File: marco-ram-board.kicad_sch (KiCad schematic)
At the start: 0 parts

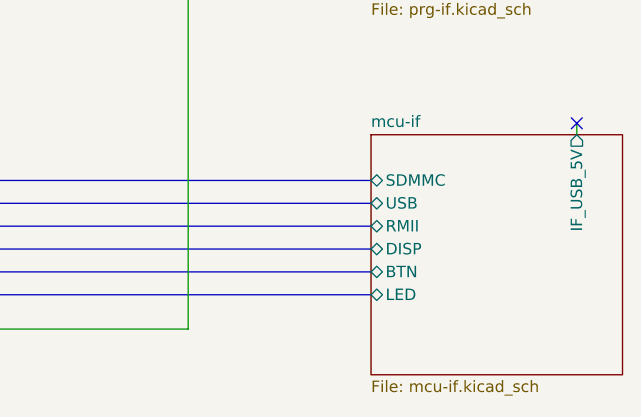
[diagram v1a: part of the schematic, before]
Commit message: Fix led current limiting resistor values.
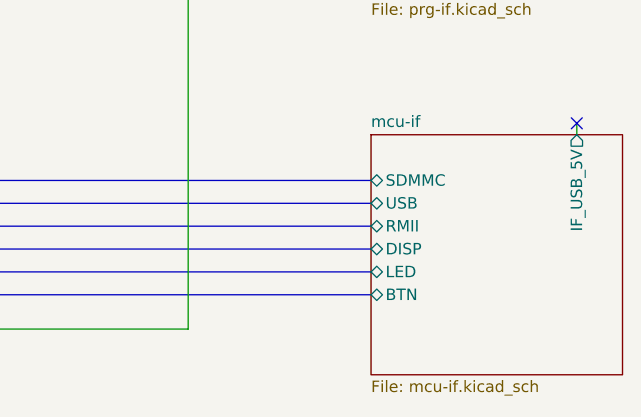
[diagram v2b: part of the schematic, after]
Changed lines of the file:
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@@
+    (stroke (width 0) (type default) (color 0 0 0 0))
+  )
+  (bus (pts (xy 163.83 82.55) (xy 208.28 82.55))
+    (stroke (width 0) (type default) (color 0 0 0 0))
+  )
+  (wire (pts (xy 231.14 118.11) (xy 231.14 119.38))
+    (stroke (width 0) (type default) (color 0 0 0 0))
+  )
+  (wire (pts (xy 187.96 140.97) (xy 163.83 140.97))
+    (stroke (width 0) (type default) (color 0 0 0 0))
+  )
+  (wire (pts (xy 187.96 99.06) (xy 208.28 99.06))
+    (stroke (width 0) (type default) (color 0 0 0 0))
+  )
+  (wire (pts (xy 163.83 87.63) (xy 208.28 87.63))
+    (stroke (width 0) (type default) (color 0 0 0 0))
+  )
+  (bus (pts (xy 105.41 82.55) (xy 125.73 82.55))
+    (stroke (width 0) (type default) (color 0 0 0 0))
+  )
+  (bus (pts (xy 163.83 134.62) (xy 208.28 134.62))
+    (stroke (width 0) (type default) (color 0 0 0 0))
+  )
+  (bus (pts (xy 163.83 132.08) (xy 208.28 132.08))
+    (stroke (width 0) (type default) (color 0 0 0 0))
+  )
+  (bus (pts (xy 163.83 127) (xy 208.28 127))
+    (stroke (width 0) (type default) (color 0 0 0 0))
+  )
+  (bus (pts (xy 163.83 129.54) (xy 208.28 129.54))
+    (stroke (width 0) (type default) (color 0 0 0 0))
+  )
+  (wire (pts (xy 163.83 90.17) (xy 208.28 90.17))
+    (stroke (width 0) (type default) (color 0 0 0 0))
+  )
+  (wire (pts (xy 231.14 76.2) (xy 231.14 77.47))
     (stroke (width 0) (type default) (color 0 0 0 0))
   )
   (bus (pts (xy 163.83 137.16) (xy 208.28 137.16))
-    (stroke (width 0) (type default) (color 0 0 0 0))
-  )
-  (bus (pts (xy 163.83 82.55) (xy 208.28 82.55))
-    (stroke (width 0) (type default) (color 0 0 0 0))
-  )
-  (wire (pts (xy 231.14 118.11) (xy 231.14 119.38))
-    (stroke (width 0) (type default) (color 0 0 0 0))
-  )
-  (wire (pts (xy 187.96 140.97) (xy 163.83 140.97))
-    (stroke (width 0) (type default) (color 0 0 0 0))
-  )
-  (wire (pts (xy 187.96 99.06) (xy 208.28 99.06))
-    (stroke (width 0) (type default) (color 0 0 0 0))
-  )
-  (wire (pts (xy 163.83 87.63) (xy 208.28 87.63))
-    (stroke (width 0) (type default) (color 0 0 0 0))
-  )
-  (bus (pts (xy 105.41 82.55) (xy 125.73 82.55))
-    (stroke (width 0) (type default) (color 0 0 0 0))
-  )
-  (bus (pts (xy 163.83 134.62) (xy 208.28 134.62))
-    (stroke (width 0) (type default) (color 0 0 0 0))
-  )
-  (bus (pts (xy 163.83 132.08) (xy 208.28 132.08))
-    (stroke (width 0) (type default) (color 0 0 0 0))
-  )
-  (bus (pts (xy 163.83 127) (xy 208.28 127))
-    (stroke (width 0) (type default) (color 0 0 0 0))
-  )
-  (bus (pts (xy 163.83 129.54) (xy 208.28 129.54))
-    (stroke (width 0) (type default) (color 0 0 0 0))
-  )
-  (wire (pts (xy 163.83 90.17) (xy 208.28 90.17))
-    (stroke (width 0) (type default) (color 0 0 0 0))
-  )
-  (wire (pts (xy 231.14 76.2) (xy 231.14 77.47))
     (stroke (width 0) (type default) (color 0 0 0 0))
   )
@@
       (effects (font (size 1.27 1.27)) (justify left))
     )
-    (pin "BTN" bidirectional (at 208.28 134.62 180)
-      (effects (font (size 1.27 1.27)) (justify left))
-    )
-    (pin "LED" bidirectional (at 208.28 137.16 180)
+    (pin "BTN" bidirectional (at 208.28 137.16 180)
+      (effects (font (size 1.27 1.27)) (justify left))
+    )
+    (pin "LED" bidirectional (at 208.28 134.62 180)
       (effects (font (size 1.27 1.27)) (justify left))
     )
@@
     )
     (path "/ef3f0de9-deea-4baf-8cd2-112c438774cf/e086f911-9e08-44f9-aabf-587eabb386f3"
-      (reference "R524") (unit 1) (value "4.7k") (footprint "Resistor_SMD:R_0603_1608Metric_Pad0.98x0.95mm_HandSolder")
+      (reference "R524") (unit 1) (value "1k") (footprint "Resistor_SMD:R_0603_1608Metric_Pad0.98x0.95mm_HandSolder")
     )
     (path "/ef3f0de9-deea-4baf-8cd2-112c438774cf/14e0c3db-a991-4c83-980b-8357c4d4d7a4"
-      (reference "R525") (unit 1) (value "4.7") (footprint "Resistor_SMD:R_0603_1608Metric_Pad0.98x0.95mm_HandSolder")
+      (reference "R525") (unit 1) (value "1.5k") (footprint "Resistor_SMD:R_0603_1608Metric_Pad0.98x0.95mm_HandSolder")
     )
     (path "/ef3f0de9-deea-4baf-8cd2-112c438774cf/36faf224-6d62-4451-a816-f4a91175efd8"
@@
     )
     (path "/7c962775-7ac8-4e55-b50e-b888d058fafd/a0730651-6647-4a63-a318-43f3d386b902"
-      (reference "R601") (unit 1) (value "4.7k") (footprint "Resistor_SMD:R_0603_1608Metric_Pad0.98x0.95mm_HandSolder")
+      (reference "R601") (unit 1) (value "1k") (footprint "Resistor_SMD:R_0603_1608Metric_Pad0.98x0.95mm_HandSolder")
     )
     (path "/c916b37e-aadf-4c0e-9d65-44e77380383d/efe93068-fc35-43d2-8763-3cdcf19b93ca"

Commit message: Started placement
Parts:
- added H101, H102, H103, H104: MountingHole, MountingHole:MountingHole_3.2mm_M3, symbol Mechanical:MountingHole
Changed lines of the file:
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@@
     (stroke (width 0) (type default) (color 0 0 0 0))
+  )
+  (symbol (lib_id "Mechanical:MountingHole") (at 200.66 53.34 0) (unit 1)
+    (in_bom yes) (on_board yes) (fields_autoplaced)
+    (property "Reference" "H103" (id 0) (at 203.2 52.0699 0)
+      (effects (font (size 1.27 1.27)) (justify left))
+    )
+    (property "Value" "MountingHole" (id 1) (at 203.2 54.6099 0)
+      (effects (font (size 1.27 1.27)) (justify left))
+    )
+    (property "Footprint" "MountingHole:MountingHole_3.2mm_M3" (id 2) (at 200.66 53.34 0)
+      (effects (font (size 1.27 1.27)) hide)
+    )
+    (property "Datasheet" "~" (id 3) (at 200.66 53.34 0)
+      (effects (font (size 1.27 1.27)) hide)
+    )
+  )
+  (symbol (lib_id "Mechanical:MountingHole") (at 200.66 58.42 0) (unit 1)
+    (in_bom yes) (on_board yes) (fields_autoplaced)
+    (property "Reference" "H104" (id 0) (at 203.2 57.1499 0)
+      (effects (font (size 1.27 1.27)) (justify left))
+    )
+    (property "Value" "MountingHole" (id 1) (at 203.2 59.6899 0)
+      (effects (font (size 1.27 1.27)) (justify left))
+    )
+    (property "Footprint" "MountingHole:MountingHole_3.2mm_M3" (id 2) (at 200.66 58.42 0)
+      (effects (font (size 1.27 1.27)) hide)
+    )
+    (property "Datasheet" "~" (id 3) (at 200.66 58.42 0)
+      (effects (font (size 1.27 1.27)) hide)
+    )
+  )
+  (symbol (lib_id "Mechanical:MountingHole") (at 200.66 48.26 0) (unit 1)
+    (in_bom yes) (on_board yes) (fields_autoplaced)
+    (property "Reference" "H102" (id 0) (at 203.2 46.9899 0)
+      (effects (font (size 1.27 1.27)) (justify left))
+    )
+    (property "Value" "MountingHole" (id 1) (at 203.2 49.5299 0)
+      (effects (font (size 1.27 1.27)) (justify left))
+    )
+    (property "Footprint" "MountingHole:MountingHole_3.2mm_M3" (id 2) (at 200.66 48.26 0)
+      (effects (font (size 1.27 1.27)) hide)
+    )
+    (property "Datasheet" "~" (id 3) (at 200.66 48.26 0)
+      (effects (font (size 1.27 1.27)) hide)
+    )
+  )
+  (symbol (lib_id "Mechanical:MountingHole") (at 200.66 43.18 0) (unit 1)
+    (in_bom yes) (on_board yes) (fields_autoplaced)
+    (property "Reference" "H101" (id 0) (at 203.2 41.9099 0)
+      (effects (font (size 1.27 1.27)) (justify left))
+    )
+    (property "Value" "MountingHole" (id 1) (at 203.2 44.4499 0)
+      (effects (font (size 1.27 1.27)) (justify left))
+    )
+    (property "Footprint" "MountingHole:MountingHole_3.2mm_M3" (id 2) (at 200.66 43.18 0)
+      (effects (font (size 1.27 1.27)) hide)
+    )
+    (property "Datasheet" "~" (id 3) (at 200.66 43.18 0)
+      (effects (font (size 1.27 1.27)) hide)
+    )
   )
   (sheet (at 64.77 77.47) (size 40.64 68.58) (fields_autoplaced)
@@
       (reference "FB501") (unit 1) (value "FerriteBead") (footprint "Inductor_SMD:L_0603_1608Metric_Pad1.05x0.95mm_HandSolder")
     )
+    (path "/a61d3367-e3ba-4684-bf37-a834250575f8"
+      (reference "H101") (unit 1) (value "MountingHole") (footprint "MountingHole:MountingHole_3.2mm_M3")
+    )
+    (path "/932c0d32-af59-4449-a243-2f2fae607baf"
+      (reference "H102") (unit 1) (value "MountingHole") (footprint "MountingHole:MountingHole_3.2mm_M3")
+    )
+    (path "/194fe233-8bf5-4d85-bf79-ef616629bb38"
+      (reference "H103") (unit 1) (value "MountingHole") (footprint "MountingHole:MountingHole_3.2mm_M3")
+    )
+    (path "/3febbed2-c5e0-4559-a7ac-28c1e851d019"
+      (reference "H104") (unit 1) (value "MountingHole") (footprint "MountingHole:MountingHole_3.2mm_M3")
+    )
     (path "/560cd6d2-0a02-4f8b-872b-85e24c6da3bb/347d33d9-c321-4d8b-982e-19c6ba84f804"

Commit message: Add worksheet template with PoliMi logo.
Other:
- title: (none) -> MARCO RAM Board
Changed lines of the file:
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@@
 (kicad_sch (version 20211123) (generator eeschema)
   (paper "A4")
+  (title_block
+    (title "MARCO RAM Board")
+    (rev "1")
+    (comment 9 "Root sheet")
+  )
   (no_connect (at 231.14 76.2))
   (no_connect (at 231.14 118.11))
